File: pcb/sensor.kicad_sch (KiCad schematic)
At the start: 15 parts, among them J2 Conn_01x05, U1 pmw3360-t2qu, U2 TLV70018_SOT23-5

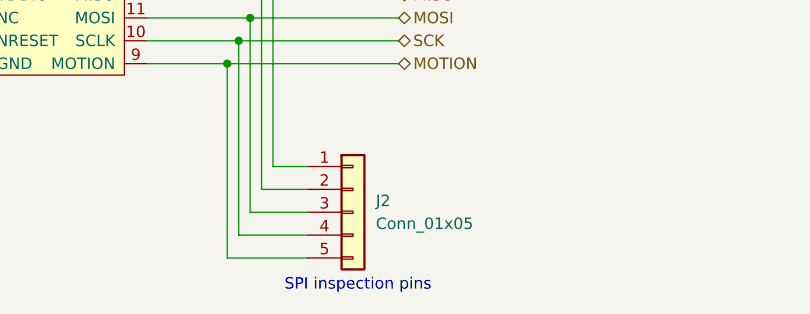
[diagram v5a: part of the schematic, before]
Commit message: - cleaned up schematics - roughly arranged components on pcb - added pcb outline
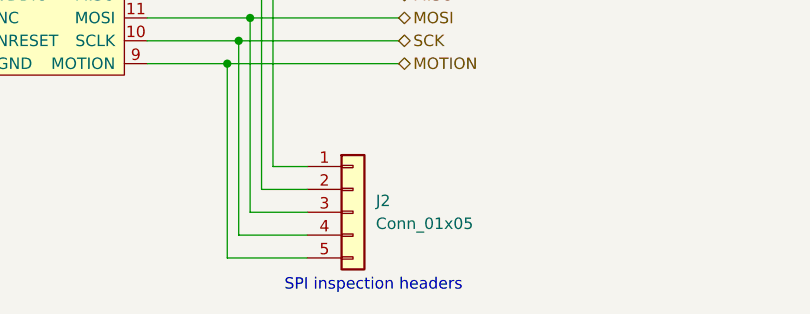
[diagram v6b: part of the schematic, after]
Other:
- note added: "SPI inspection headers"
- note removed: "SPI inspection pins"
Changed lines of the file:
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@@
     (effects (font (size 1.27 1.27)) (justify left bottom))
   )
-  (text "SPI inspection pins" (at 96.52 148.59 0)
+  (text "SPI inspection headers" (at 96.52 148.59 0)
     (effects (font (size 1.27 1.27)) (justify left bottom))
   )
@@
   (symbol (lib_id "power:+1V8") (at 251.46 119.38 0) (unit 1)
     (in_bom yes) (on_board yes) (fields_autoplaced)
-    (property "Reference" "#PWR?" (id 0) (at 251.46 123.19 0)
-      (effects (font (size 1.27 1.27)) hide)
-    )
+    (property "Reference" "#PWR0101" (id 0) (at 251.46 123.19 0)
+      (effects (font (size 1.27 1.27)) hide)
+    )
